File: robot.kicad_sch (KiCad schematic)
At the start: 22 parts, among them J3 Programming, J5 Switches, SW1 Reset, SW2 Action, SW3 KILL, SW4 Flash, SW6 OPTION, U1 ESP32-WROOM-32D, U8 ESP32-S3-WROOM-1

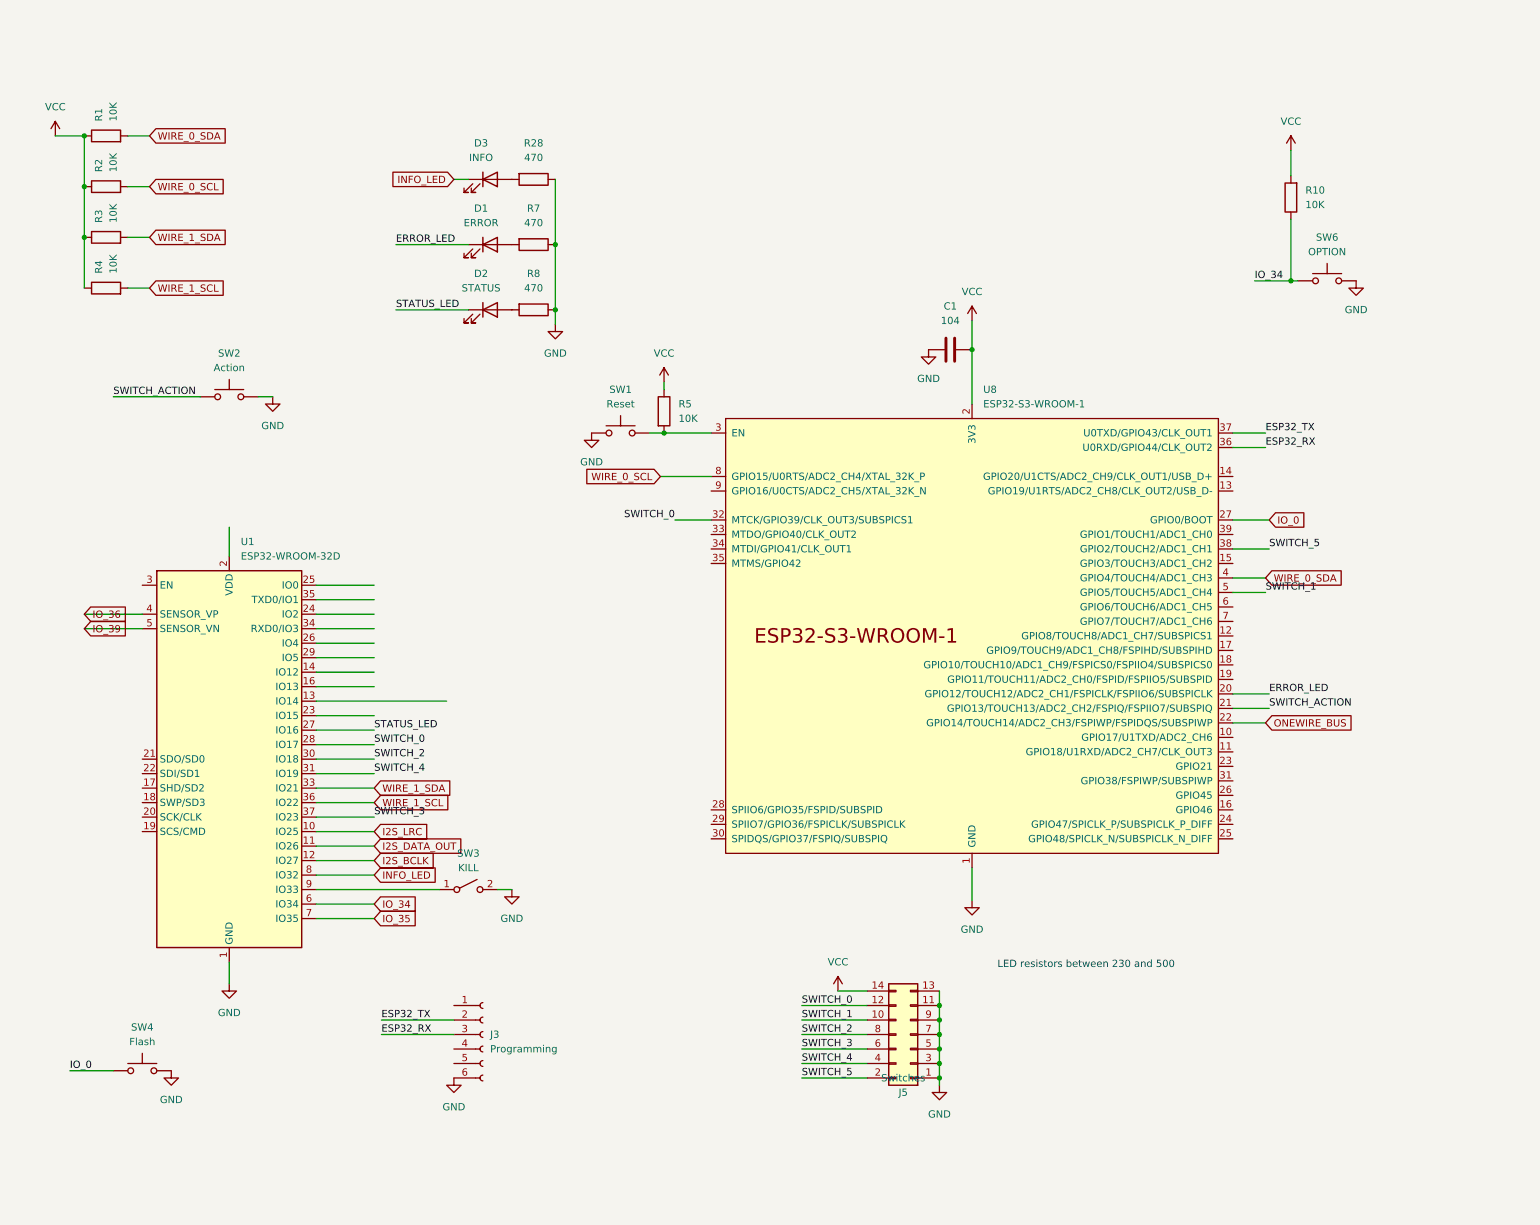
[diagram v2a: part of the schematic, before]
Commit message: Removed old ESP32, added ESP32 S3.
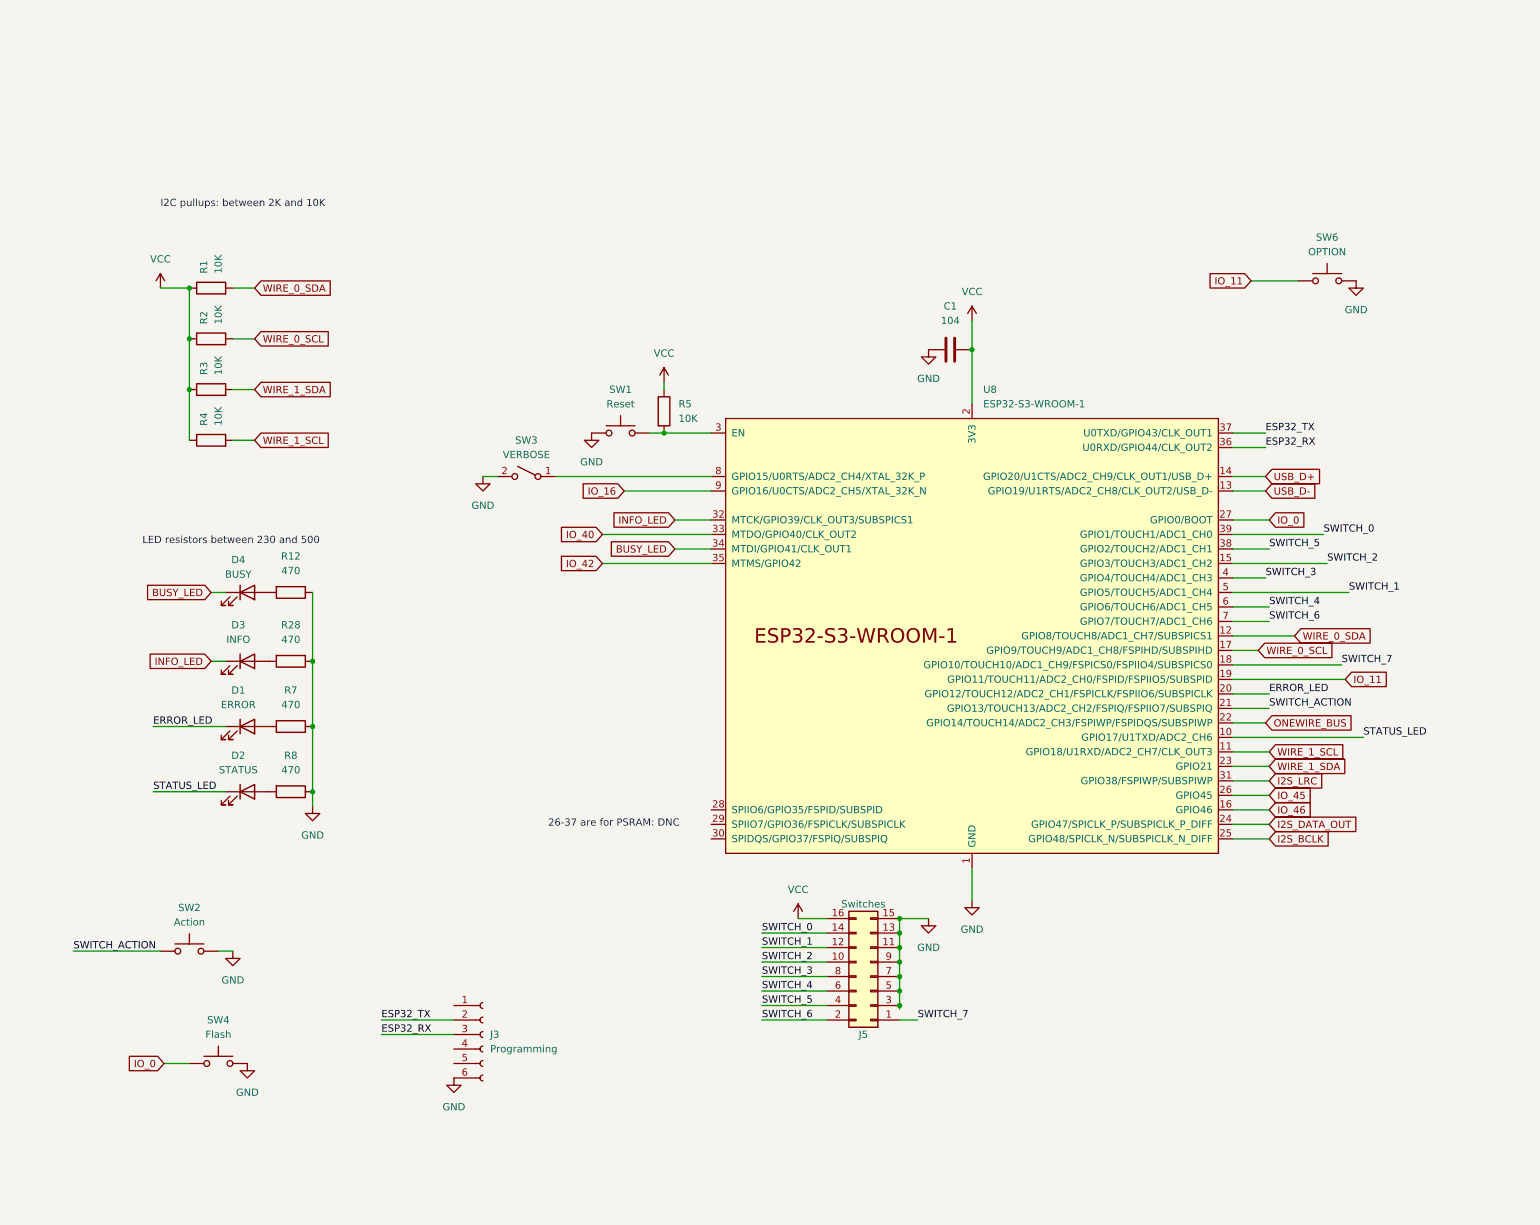
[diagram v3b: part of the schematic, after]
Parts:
- removed R10: 10K, Resistor_SMD:R_1206_3216Metric_Pad1.30x1.75mm_HandSolder, symbol Device:R
- removed U1: ESP32-WROOM-32D, RF_Module:ESP32-WROOM-32, symbol RF_Module:ESP32-WROOM-32D
- added D4: BUSY, LED_SMD:LED_1206_3216Metric_Pad1.42x1.75mm_HandSolder, symbol Device:LED
- added R12: 470, Resistor_SMD:R_1206_3216Metric_Pad1.30x1.75mm_HandSolder, symbol Device:R
- J5: footprint Connector_PinSocket_2.54mm:PinSocket_2x07_P2.54mm_Vertical -> Connector_PinSocket_2.54mm:PinSocket_2x08_P2.54mm_Vertical; symbol Connector_Generic:Conn_02x07_Odd_Even -> Connector_Generic:Conn_02x08_Odd_Even
- SW3: value KILL -> VERBOSE
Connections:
- net IO_34 is gone; now on net IO_11: SW6.1
- net GND: now also J5.15 (Pin_15), R12.1; no longer J5.1 (Pin_1)
- net I2S_BCLK: now also U8.25 (GPIO48/SPICLK_N/SUBSPICLK_N_DIFF)
- net I2S_DATA_OUT: now also U8.24 (GPIO47/SPICLK_P/SUBSPICLK_P_DIFF)
- net I2S_LRC: now also U8.31 (GPIO38/FSPIWP/SUBSPIWP)
- net INFO_LED: now also U8.32 (MTCK/GPIO39/CLK_OUT3/SUBSPICS1)
- net STATUS_LED: now also U8.10 (GPIO17/U1TXD/ADC2_CH6)
- net SWITCH_0: now also J5.14 (Pin_14), U8.39 (GPIO1/TOUCH1/ADC1_CH0); no longer J5.12 (Pin_12), U8.32 (MTCK/GPIO39/CLK_OUT3/SUBSPICS1)
- net SWITCH_1: now also J5.12 (Pin_12); no longer J5.10 (Pin_10)
- net SWITCH_2: now also J5.10 (Pin_10), U8.15 (GPIO3/TOUCH3/ADC1_CH2); no longer J5.8 (Pin_8)
- net SWITCH_3: now also J5.8 (Pin_8), U8.4 (GPIO4/TOUCH4/ADC1_CH3); no longer J5.6 (Pin_6)
- net SWITCH_4: now also J5.6 (Pin_6), U8.6 (GPIO6/TOUCH6/ADC1_CH5); no longer J5.4 (Pin_4)
- net SWITCH_5: now also J5.4 (Pin_4); no longer J5.2 (Pin_2)
- net VCC: now also J5.16 (Pin_16); no longer J5.14 (Pin_14)
- net WIRE_0_SCL: now also U8.17 (GPIO9/TOUCH9/ADC1_CH8/FSPIHD/SUBSPIHD); no longer U8.8 (GPIO15/U0RTS/ADC2_CH4/XTAL_32K_P)
- net WIRE_0_SDA: now also U8.12 (GPIO8/TOUCH8/ADC1_CH7/SUBSPICS1); no longer U8.4 (GPIO4/TOUCH4/ADC1_CH3)
- net WIRE_1_SCL: now also U8.11 (GPIO18/U1RXD/ADC2_CH7/CLK_OUT3)
- net WIRE_1_SDA: now also U8.23 (GPIO21)
- net at SW3.1 (A): now also U8.8 (GPIO15/U0RTS/ADC2_CH4/XTAL_32K_P)
- net USB_D-: now reaches U8.13 (GPIO19/U1RTS/ADC2_CH8/CLK_OUT2/USB_D-)
- net USB_D+: now reaches U8.14 (GPIO20/U1CTS/ADC2_CH9/CLK_OUT1/USB_D+)
- net IO_46: now reaches U8.16 (GPIO46)
- net SWITCH_7: now reaches U8.18 (GPIO10/TOUCH10/ADC1_CH9/FSPICS0/FSPIIO4/SUBSPICS0)
- net SWITCH_7: now also J5.1 (Pin_1)
- net IO_11: now reaches U8.19 (GPIO11/TOUCH11/ADC2_CH0/FSPID/FSPIIO5/SUBSPID)
- net IO_45: now reaches U8.26 (GPIO45)
- net IO_40: now reaches U8.33 (MTDO/GPIO40/CLK_OUT2)
- net BUSY_LED: now reaches U8.34 (MTDI/GPIO41/CLK_OUT1)
- net BUSY_LED: now also D4.1 (K)
- net IO_42: now reaches U8.35 (MTMS/GPIO42)
- net SWITCH_6: now reaches U8.7 (GPIO7/TOUCH7/ADC1_CH6)
- net SWITCH_6: now also J5.2 (Pin_2)
- net IO_16: now reaches U8.9 (GPIO16/U0CTS/ADC2_CH5/XTAL_32K_N)
- new net: D4.2 (A), R12.2
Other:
- note added: "26-37 are for PSRAM: DNC"
- note added: "I2C pullups: between 2K and 10K"
- moved on the sheet: D1, D2, D3, R1, R2, R28, R3, R4, R7, R8, SW2, SW3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

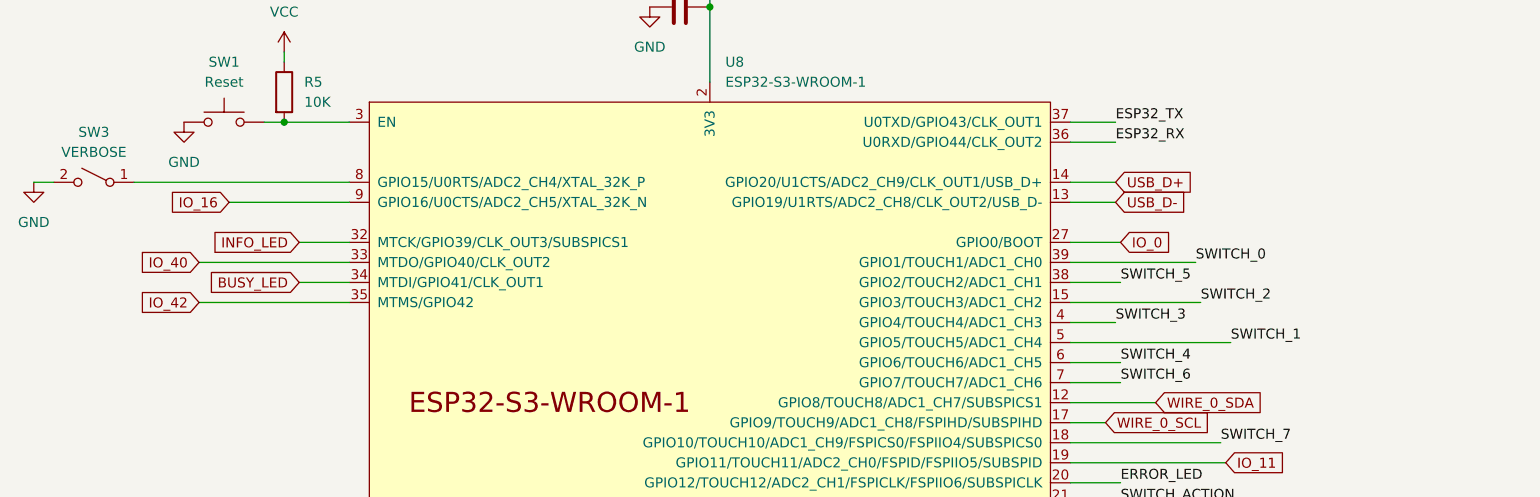
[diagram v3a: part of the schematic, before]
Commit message: Switched out GPIO3 for GPIO16 because it is a strapping pin with no pullup.
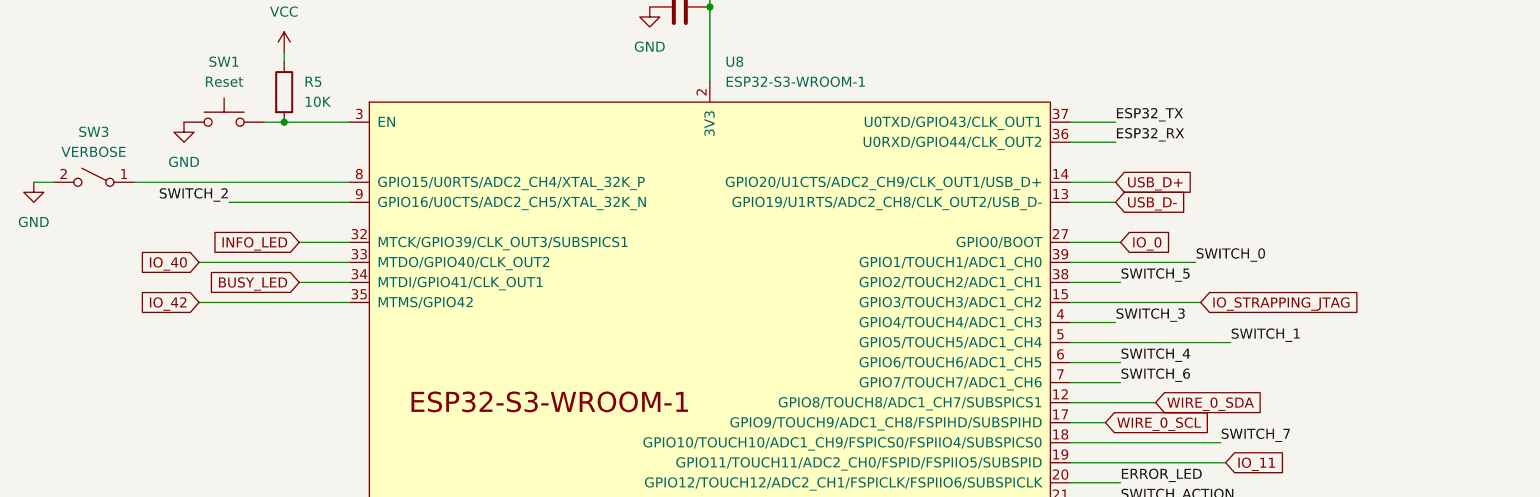
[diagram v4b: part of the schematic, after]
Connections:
- net IO_16 is gone; now on net SWITCH_2: U8.9 (GPIO16/U0CTS/ADC2_CH5/XTAL_32K_N)
- net SWITCH_2: no longer U8.15 (GPIO3/TOUCH3/ADC1_CH2)
- new net IO_STRAPPING_JTAG: U8.15 (GPIO3/TOUCH3/ADC1_CH2)
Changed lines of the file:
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@@
     (effects (font (size 1.27 1.27)) (justify left bottom))
   )
-  (label "SWITCH_2" (at 238.125 99.06 0) (fields_autoplaced)
-    (effects (font (size 1.27 1.27)) (justify left bottom))
+  (label "SWITCH_2" (at 114.935 86.36 180) (fields_autoplaced)
+    (effects (font (size 1.27 1.27)) (justify right bottom))
   )
   (label "ESP32_TX" (at 227.33 76.2 0) (fields_autoplaced)
@@
     )
   )
-  (global_label "IO_16" (shape input) (at 114.935 86.36 180) (fields_autoplaced)
-    (effects (font (size 1.27 1.27)) (justify right))
-    (property "Intersheetrefs" "${INTERSHEET_REFS}" (at 106.7073 86.36 0)
-      (effects (font (size 1.27 1.27)) (justify right) hide)
+  (global_label "IO_STRAPPING_JTAG" (shape input) (at 238.125 99.06 0) (fields_autoplaced)
+    (effects (font (size 1.27 1.27)) (justify left))
+    (property "Intersheetrefs" "${INTERSHEET_REFS}" (at 259.4761 99.06 0)
+      (effects (font (size 1.27 1.27)) (justify left) hide)
     )
   )

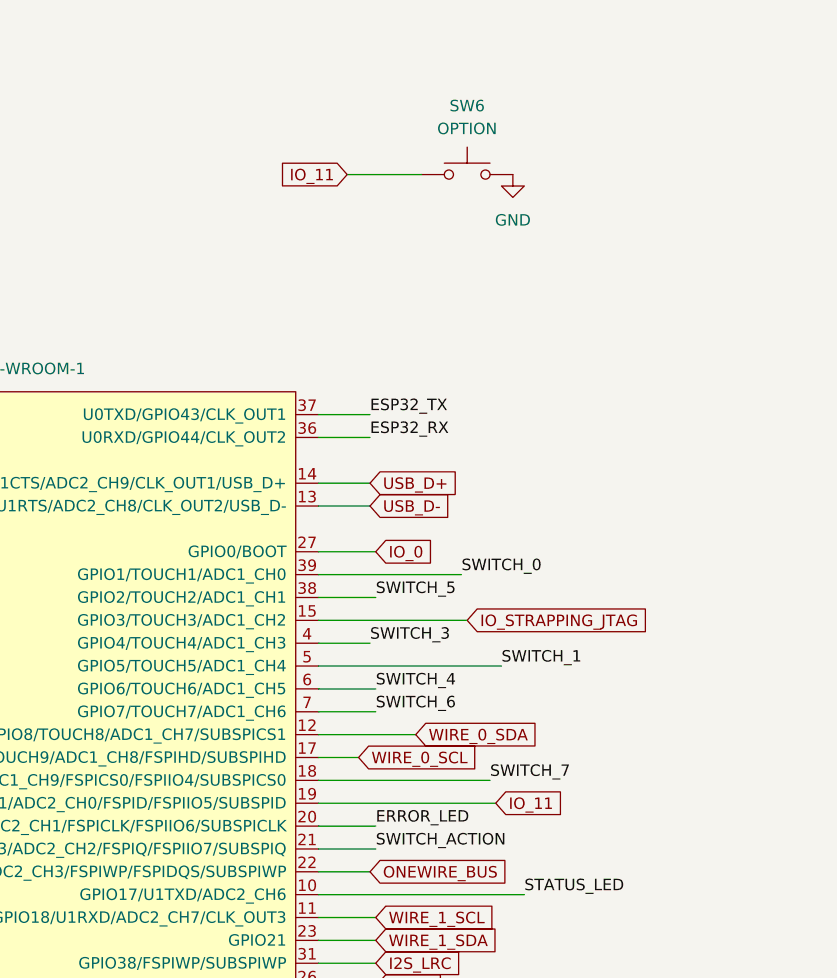
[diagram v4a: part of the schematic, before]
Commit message: Switched a few pins which were glitchy in on the hardware to known good pins. May have just been a faulty ESP32, but just to be sure.
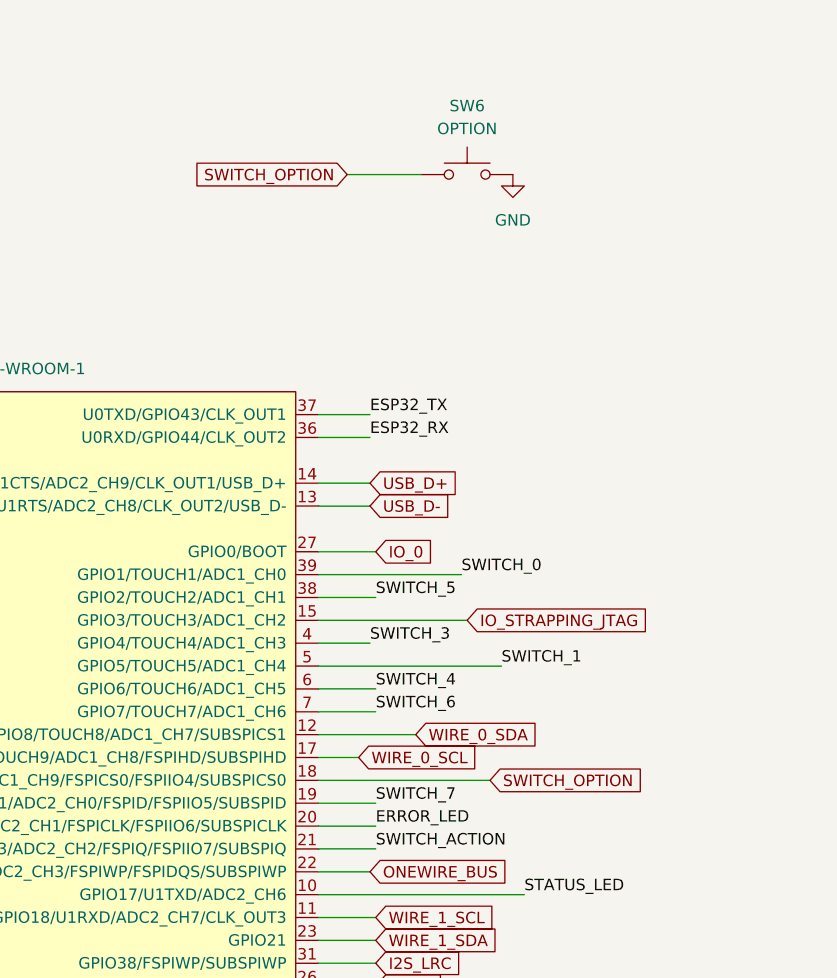
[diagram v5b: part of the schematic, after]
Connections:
- net SWITCH_7: now also U8.19 (GPIO11/TOUCH11/ADC2_CH0/FSPID/FSPIIO5/SUBSPID); no longer U8.18 (GPIO10/TOUCH10/ADC1_CH9/FSPICS0/FSPIIO4/SUBSPICS0)
- net IO_11 renamed SWITCH_OPTION
- net SWITCH_OPTION: now also U8.18 (GPIO10/TOUCH10/ADC1_CH9/FSPICS0/FSPIIO4/SUBSPICS0); no longer U8.19 (GPIO11/TOUCH11/ADC2_CH0/FSPID/FSPIIO5/SUBSPID)
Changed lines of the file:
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@@
     (stroke (width 0) (type default))
   )
-  (wire (pts (xy 221.615 119.38) (xy 241.3 119.38))
+  (wire (pts (xy 221.615 119.38) (xy 227.965 119.38))
     (stroke (width 0) (type default))
   )
@@
     (effects (font (size 1.27 1.27)) (justify left bottom))
   )
-  (label "SWITCH_7" (at 240.665 116.84 0) (fields_autoplaced)
+  (label "SWITCH_7" (at 227.965 119.38 0) (fields_autoplaced)
     (effects (font (size 1.27 1.27)) (justify left bottom))
   )
@@
     )
   )
-  (global_label "IO_11" (shape input) (at 224.79 49.53 180) (fields_autoplaced)
-    (effects (font (size 1.27 1.27)) (justify right))
-    (property "Intersheetrefs" "${INTERSHEET_REFS}" (at 216.5623 49.53 0)
+  (global_label "SWITCH_OPTION" (shape input) (at 224.79 49.53 180) (fields_autoplaced)
+    (effects (font (size 1.27 1.27)) (justify right))
+    (property "Intersheetrefs" "${INTERSHEET_REFS}" (at 207.2489 49.53 0)
       (effects (font (size 1.27 1.27)) (justify right) hide)
     )
@@
     )
   )
-  (global_label "IO_11" (shape input) (at 241.3 119.38 0) (fields_autoplaced)
-    (effects (font (size 1.27 1.27)) (justify left))
-    (property "Intersheetrefs" "${INTERSHEET_REFS}" (at 249.5277 119.38 0)
-      (effects (font (size 1.27 1.27)) (justify left) hide)
-    )
+  (global_label "SWITCH_OPTION" (shape input) (at 240.665 116.84 0) (fields_autoplaced)
+    (effects (font (size 1.27 1.27)) (justify left))
+    (property "Intersheetrefs" "${INTERSHEET_REFS}" (at 258.2061 116.84 0)
+      (effects (font (size 1.27 1.27)) (justify left) hide)
+    )
